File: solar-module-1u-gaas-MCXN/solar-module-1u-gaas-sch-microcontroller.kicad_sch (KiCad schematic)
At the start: 43 parts, among them U1 MCXN947VKLT, U11 TCAN330, U2 TMP101NA/3KSLOTTED, U7 TMP101NA/3KSLOTTED, Y2 24 MHz

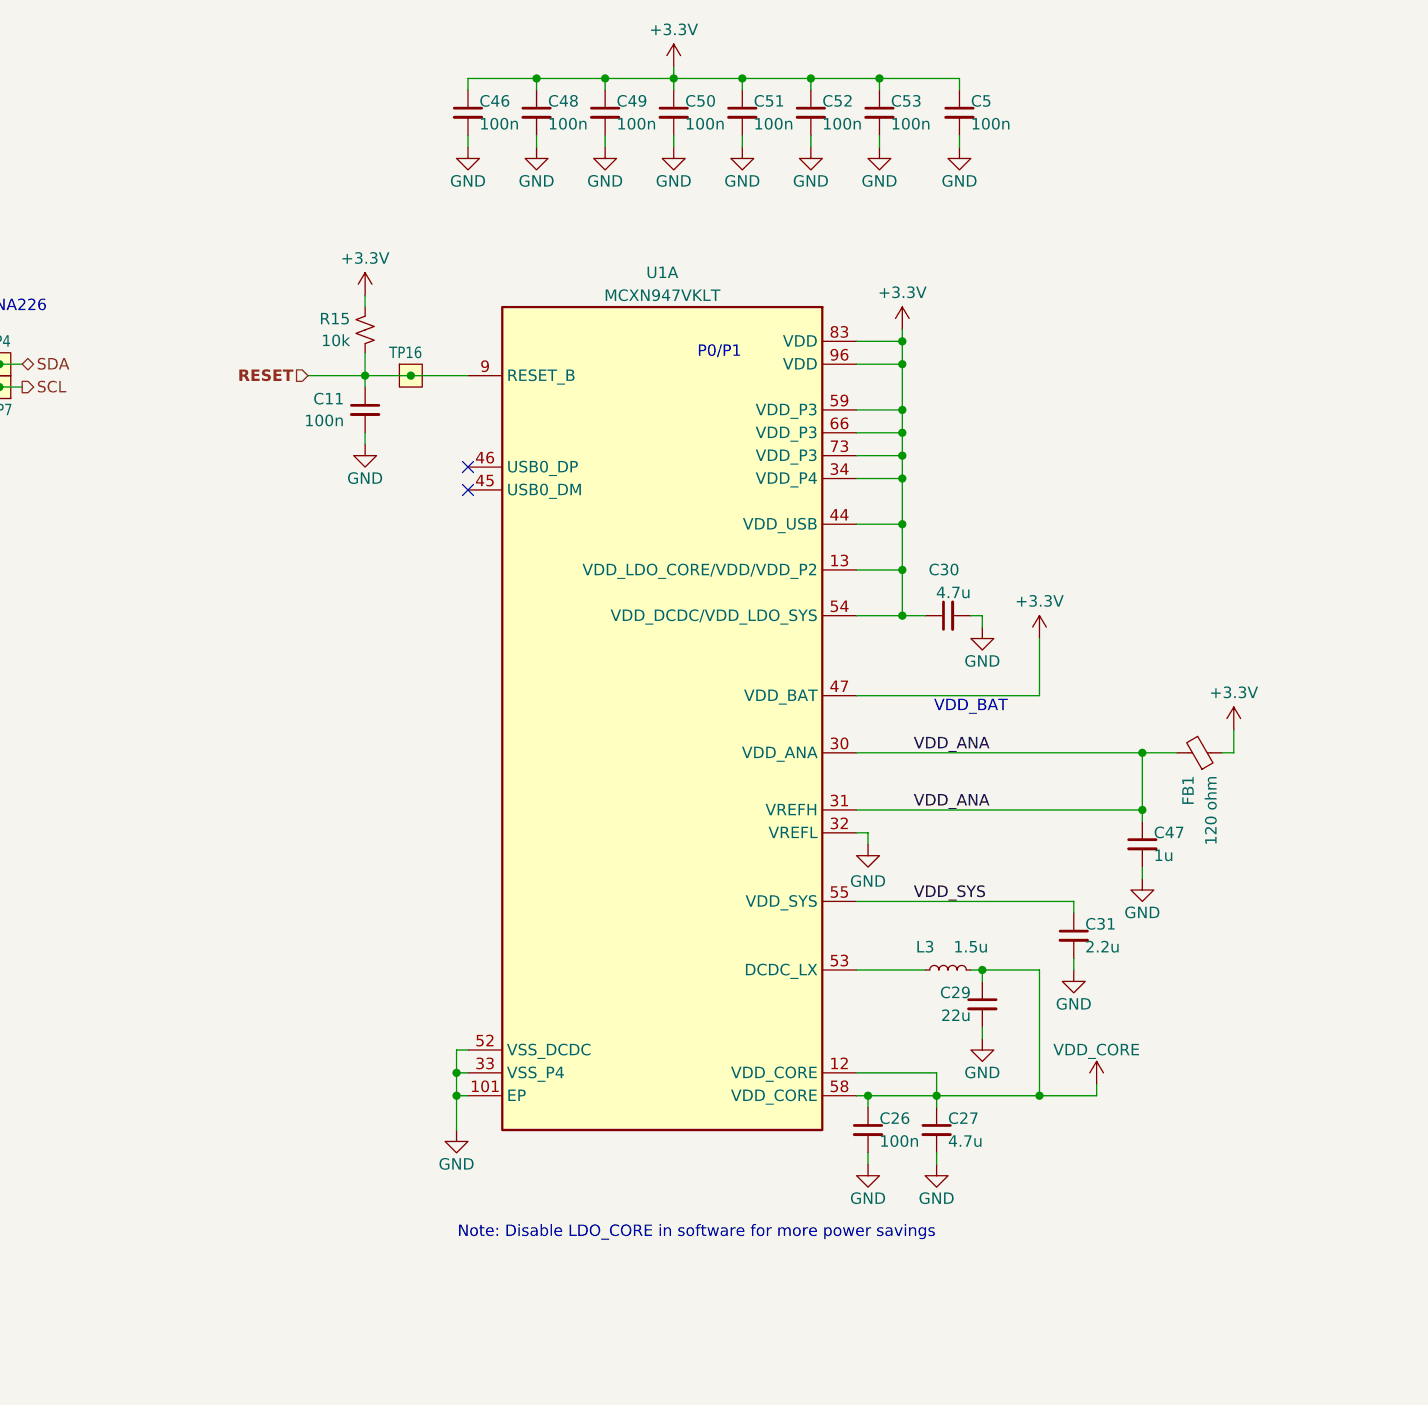
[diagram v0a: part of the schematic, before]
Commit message: Solar Module with GaAs Cells and MCXN processor v1.1
Fixed BOM, fixed solar connector sync between brd/sch, routed UART lines to the connector, untented vias for venting. Sent to fab.
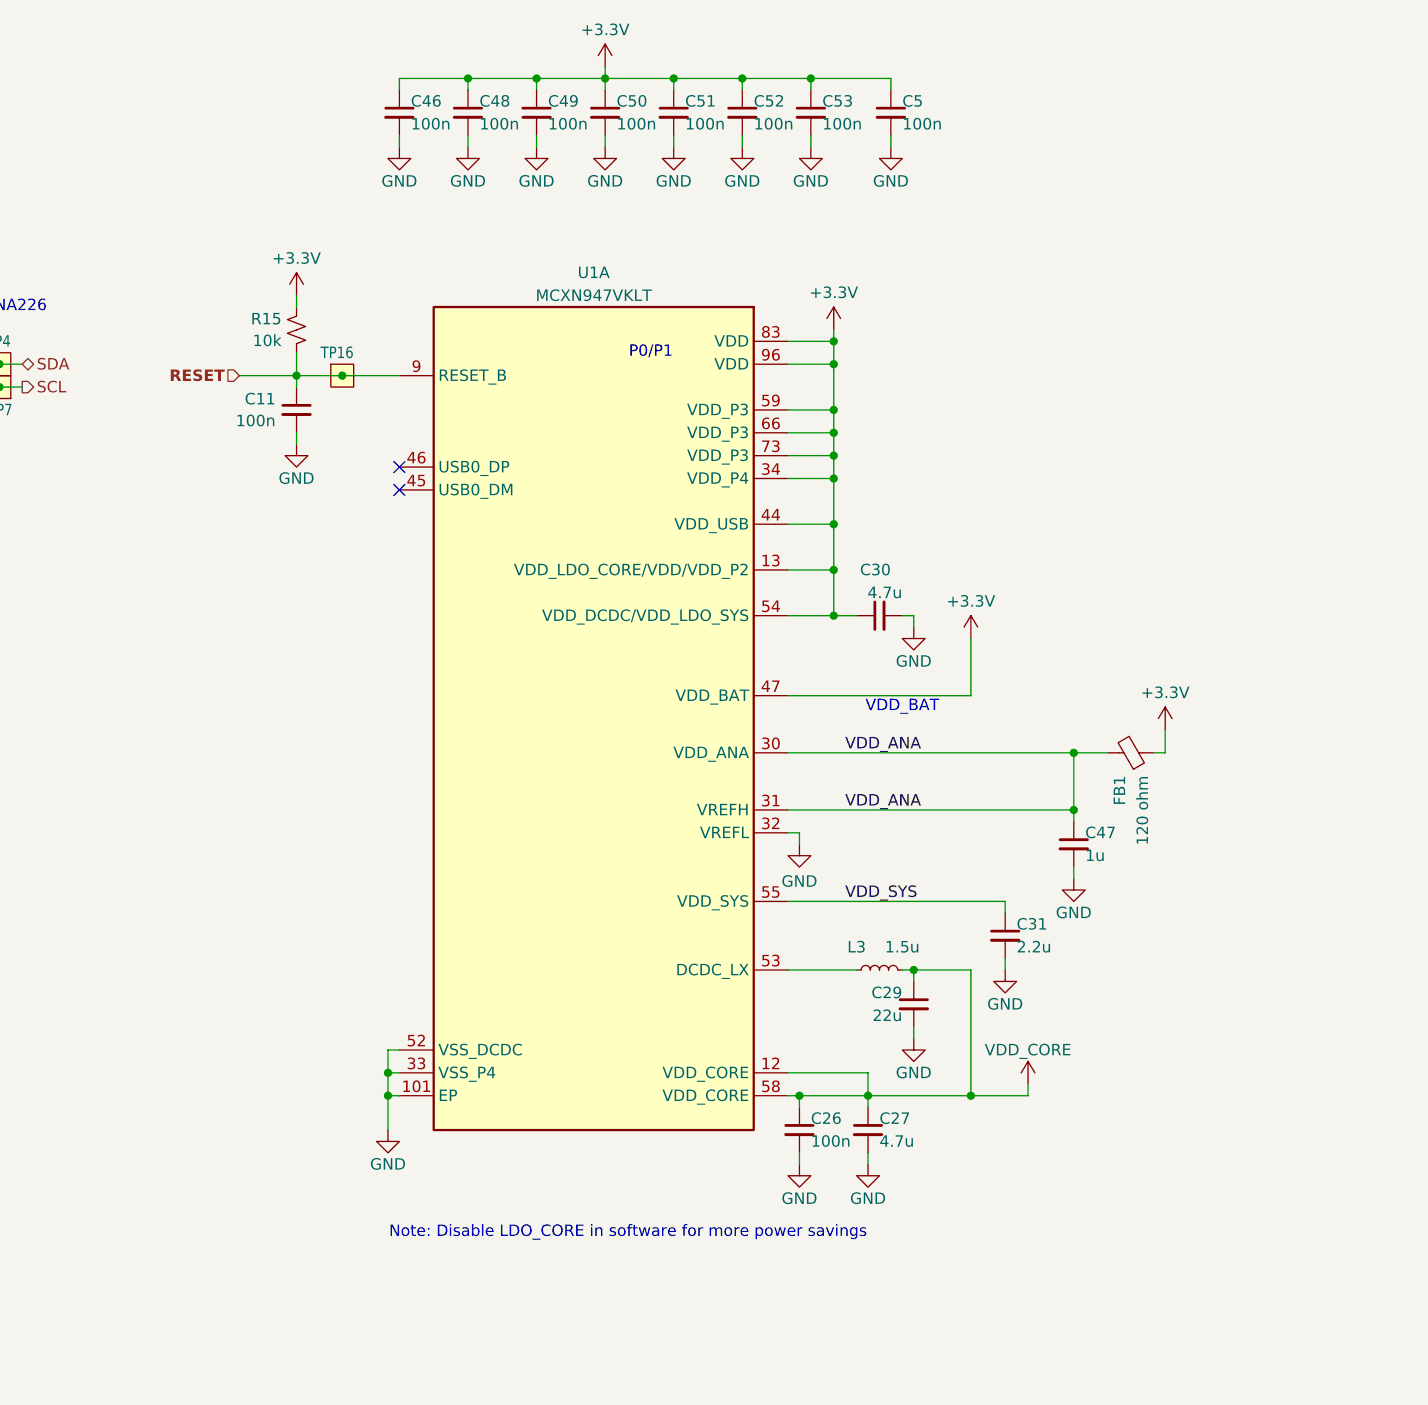
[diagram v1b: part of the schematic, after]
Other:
- moved on the sheet: C11, C26, C27, C29, C30, C31, C46, C47, C48, C49, C5, C50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
